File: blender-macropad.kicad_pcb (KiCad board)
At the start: 2 copper layers, 60 x 70 mm, 29 parts, among them J1 Conn_02x12_Counter_Clockwise, J2 Conn_01x07, SW1 SW_Push, SW10 SW_Push, SW11 SW_Push, SW12 SW_Push, SW13 RotaryEncoder_Switch, SW2 SW_Push, SW3 SW_Push, SW4 SW_Push, SW5 SW_Push, SW6 SW_Push, SW7 SW_Push, SW8 SW_Push, SW9 SW_Push

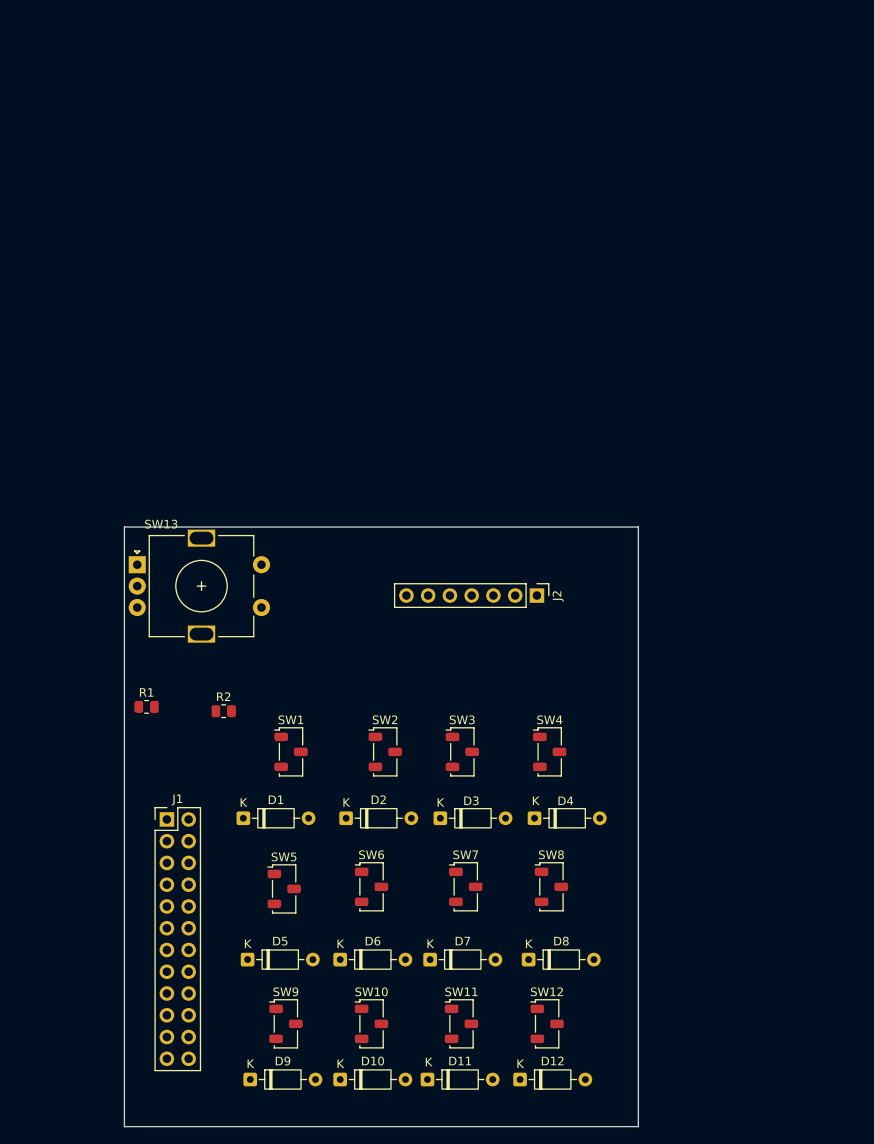
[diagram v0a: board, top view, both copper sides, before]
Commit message: reworked pcb layout
polished pc layout with correct dimension
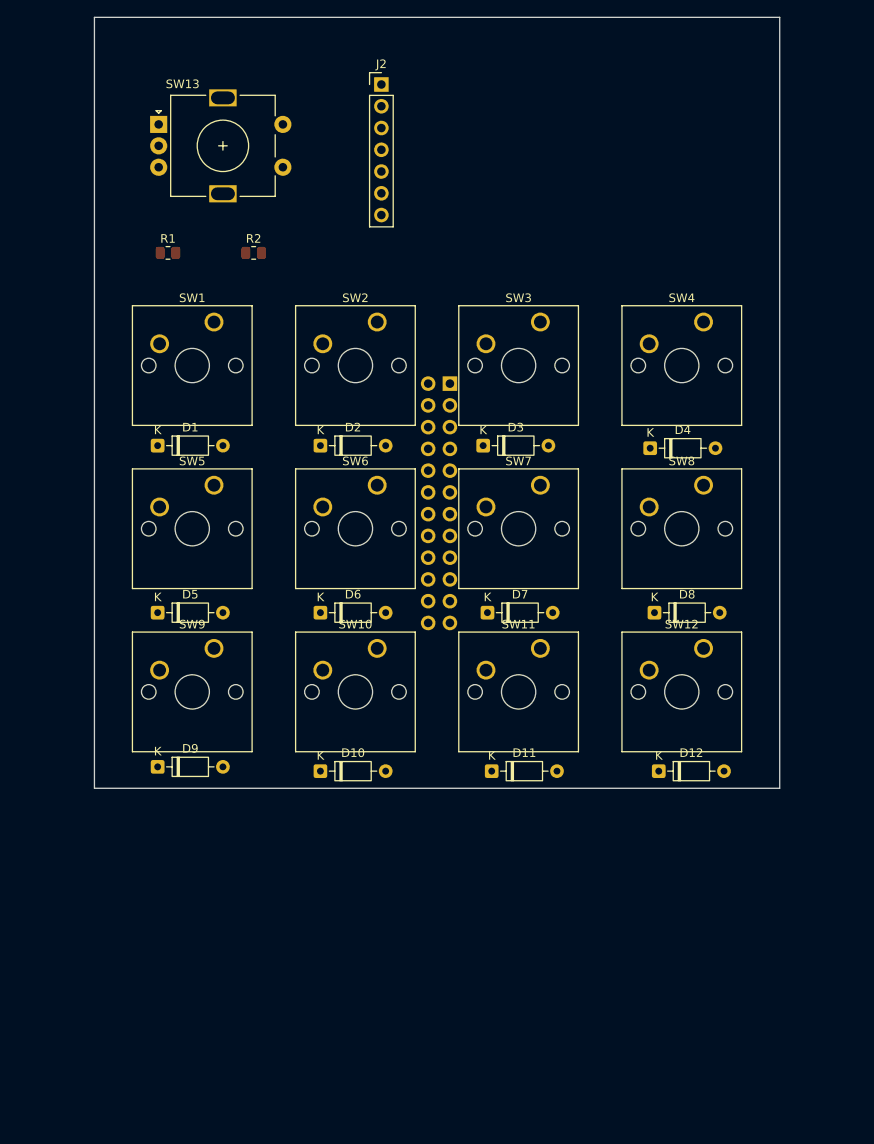
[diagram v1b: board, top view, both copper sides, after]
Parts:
- J1: moved to B.Cu
- SW1, SW10, SW11, SW12, SW2, SW3, SW4, SW5, SW6, SW7, SW8, SW9: footprint Button_Switch_SMD:Nidec_Copal_CAS-120A -> Button_Switch_Keyboard:SW_Cherry_MX_1.00u_PCB
- moved J2 62.4 mm to (207.5, 24.3), turned to 0 degrees
- moved J1 60.7 mm to (215.5, 59.3), turned to 180 degrees
- moved R2 53.6 mm to (192.6, 44.0)
- moved SW4 53.3 mm to (245.1, 52.1)
- moved R1 53.1 mm to (182.6, 44.0)
- moved SW13 51.5 mm to (181.5, 29.0)
- moved SW3 51.0 mm to (226.1, 52.1)
- moved SW1 51.0 mm to (188.0, 52.1)
- moved SW2 50.2 mm to (207.0, 52.1)
- moved SW8 50.1 mm to (245.1, 71.1)
- moved SW5 47.8 mm to (188.0, 71.1)
- moved SW7 47.7 mm to (226.1, 71.1)
- moved SW12 47.5 mm to (245.1, 90.2)
- moved SW6 46.9 mm to (207.0, 71.1)
- moved D4 45.3 mm to (238.9, 66.8)
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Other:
- board size 60 x 70 mm -> 80 x 90 mm

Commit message: Routing complete and clean DRS
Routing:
- net /GND: track 0.00 -> 96.4 mm
- net /ROW2: track 0.00 -> 84.9 mm
- net /ENC_B: track 0.00 -> 79.1 mm, vias 0 -> 2
- net /VCC: track 0.00 -> 78.6 mm
- net /ENC_A: track 0.00 -> 77.5 mm, vias 0 -> 1
- net /OLED_CS: track 0.00 -> 75.5 mm, vias 0 -> 1
- net /COL0: track 0.00 -> 73.2 mm
- net /ROW1: track 0.00 -> 71.3 mm
- net /ROW0: track 0.00 -> 69.2 mm
- net /ENC_SW: track 0.00 -> 67.6 mm, vias 0 -> 1
- net /COL3: track 0.00 -> 64.5 mm
- net /OLED_MOSI: track 0.00 -> 62.0 mm
- net /COL1: track 0.00 -> 58.8 mm
- net /OLED_CLK: track 0.00 -> 54.5 mm
- net /COL2: track 0.00 -> 51.9 mm
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
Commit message: Updated PCB
Fixed PCB
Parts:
- added H1: M3, MountingHole_3.2mm_M3, F.Cu at (170.4, 51.0)
- added H2: M3, MountingHole_3.2mm_M3, F.Cu at (257.6, 51.0)
- added H3: M3, MountingHole_3.2mm_M3, F.Cu at (170.4, 110.2)
- added H4: M3, MountingHole_3.2mm_M3, F.Cu at (257.6, 110.2)
- J1: footprint Connector_PinHeader_2.54mm:PinHeader_2x12_P2.54mm_Vertical -> Package_DIP:DIP-24_W15.24mm
- moved J1 42.1 mm to (231.6, 20.3)
- moved J2 23.8 mm to (189.4, 39.7), turned to 180 degrees
- moved R2 20.8 mm to (171.7, 44.5)
- moved SW13 12.5 mm to (169.0, 29.6)
- moved R1 11.0 mm to (171.7, 42.0)
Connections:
- J1 pad 1: /RAW -> unconnected-(J1-Pin_1-Pad1)
- J1 pad 12: /ENC_A -> unconnected-(J1-Pin_12-Pad12)
- J1 pad 13: unconnected-(J1-Pin_13-Pad13) -> /OLED_CS
- J1 pad 14: unconnected-(J1-Pin_14-Pad14) -> /OLED_MOSI
- J1 pad 15: unconnected-(J1-Pin_15-Pad15) -> /OLED_DC
- J1 pad 16: unconnected-(J1-Pin_16-Pad16) -> /OLED_CLK
- J1 pad 18: /OLED_DC -> /ENC_A
- J1 pad 19: /OLED_CS -> /ENC_B
- J1 pad 2: /GND -> unconnected-(J1-Pin_2-Pad2)
- J1 pad 20: /OLED_CLK -> /ENC_SW
- J1 pad 21: /OLED_MOSI -> /VCC
- J1 pad 22: /ENC_SW -> unconnected-(J1-Pin_22-Pad22)
- J1 pad 23: /ENC_B -> /GND
- J1 pad 24: /GND -> unconnected-(J1-Pin_24-Pad24)
- J1 pad 3: /RST -> /GND
- J1 pad 4: /VCC -> /GND
- J2 pad 1: /VCC -> /GND
- J2 pad 2: /GND -> /VCC
- J2 pad 3: /OLED_MOSI -> /OLED_CLK
- J2 pad 4: /OLED_CLK -> /OLED_MOSI
- J2 pad 5: /OLED_CS -> /OLED_RST
- J2 pad 7: /OLED_RST -> /OLED_CS
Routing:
- net /COL0: track 73.2 -> 112.9 mm
- net /ROW2: track 84.9 -> 119.3 mm
- net /ROW1: track 71.3 -> 103.4 mm
- net /OLED_CS: track 75.5 -> 45.0 mm, vias 1 -> 0
- net /ENC_SW: track 67.6 -> 37.6 mm, vias 1 -> 0
- net /OLED_MOSI: track 62.0 -> 32.6 mm
- net /VCC: track 78.6 -> 52.0 mm
- net /COL1: track 58.8 -> 84.6 mm
- net /COL2: track 51.9 -> 71.1 mm
- net /OLED_CLK: track 54.5 -> 35.9 mm
- net /ENC_A: track 77.5 -> 61.2 mm
- net /ENC_B: track 79.1 -> 63.8 mm, vias 2 -> 0
- net /ROW0: track 69.2 -> 84.4 mm
- net /GND: track 96.4 -> 82.8 mm
- net /OLED_DC: track 44.8 -> 37.0 mm
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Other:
- board size 80 x 90 mm -> 98 x 99.2 mm
- board text added: "OLED 2.08" 72.5x27.24"
- board text added: "PARTS FACE OUT"
- board text added: "Pro Micro RP2040 (B) 17.78x33.02"
- board text added: "RAW"
- board text added: "TX0"
